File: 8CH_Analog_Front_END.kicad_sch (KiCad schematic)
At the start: 0 parts

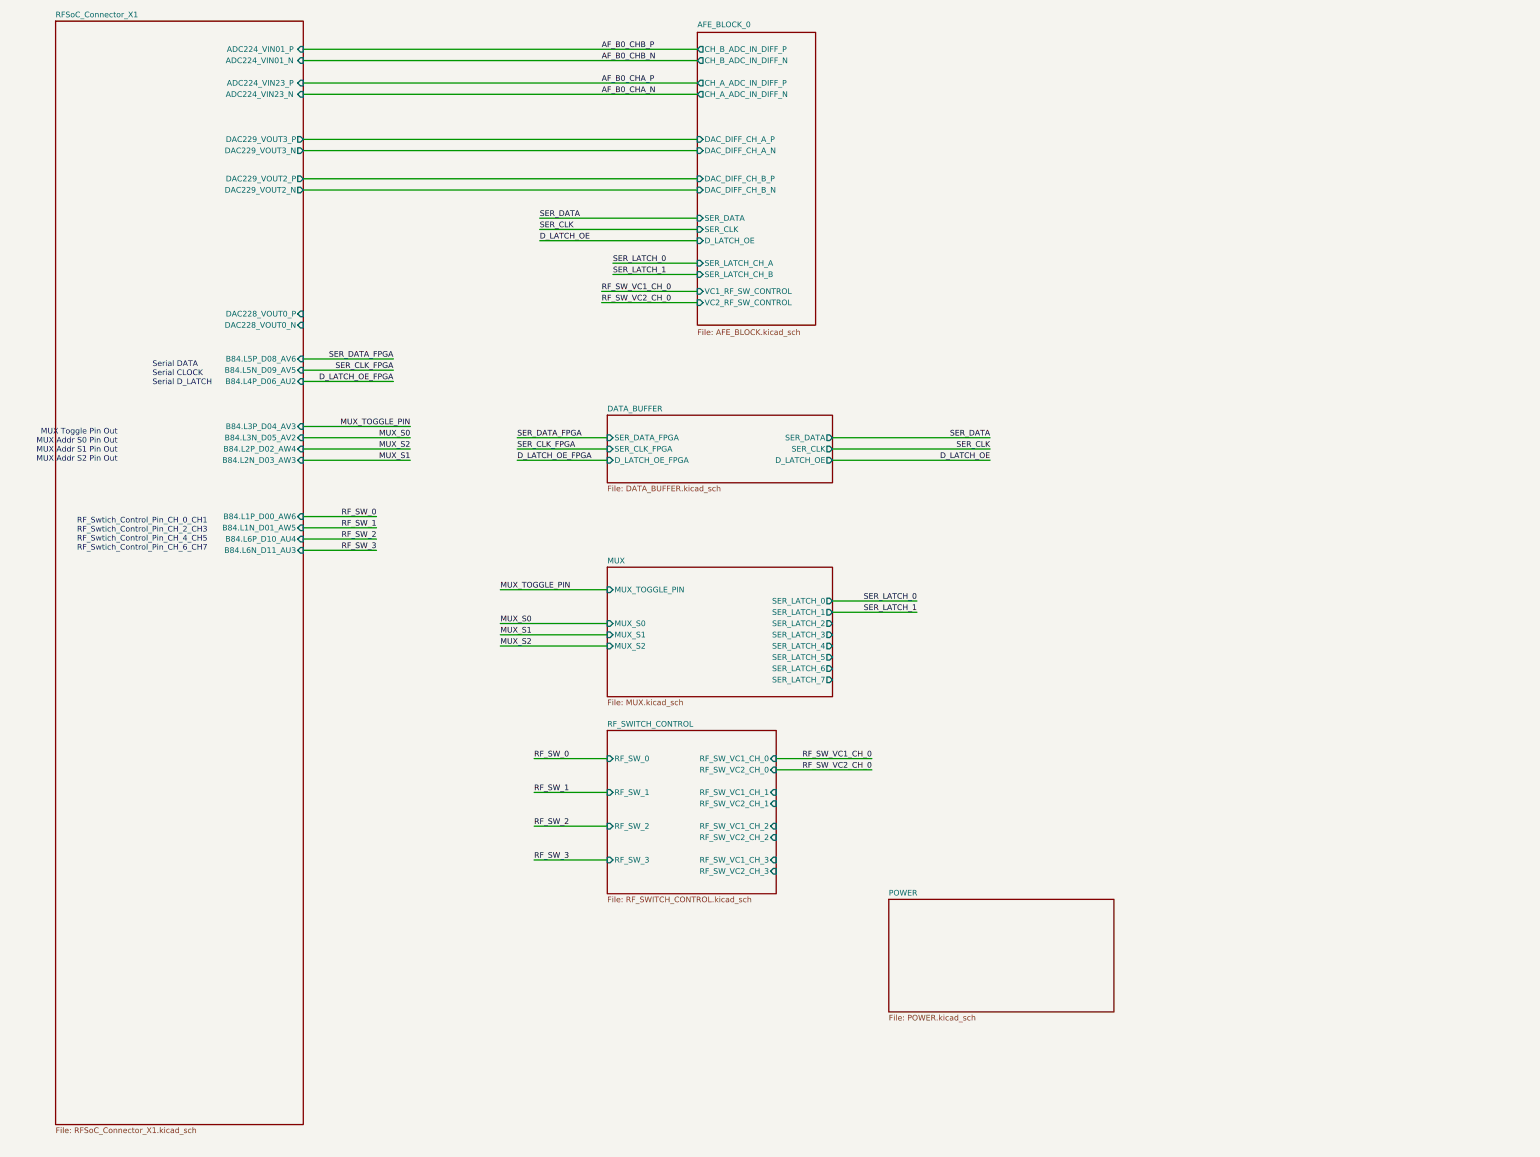
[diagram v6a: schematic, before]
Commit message: GND Vias added
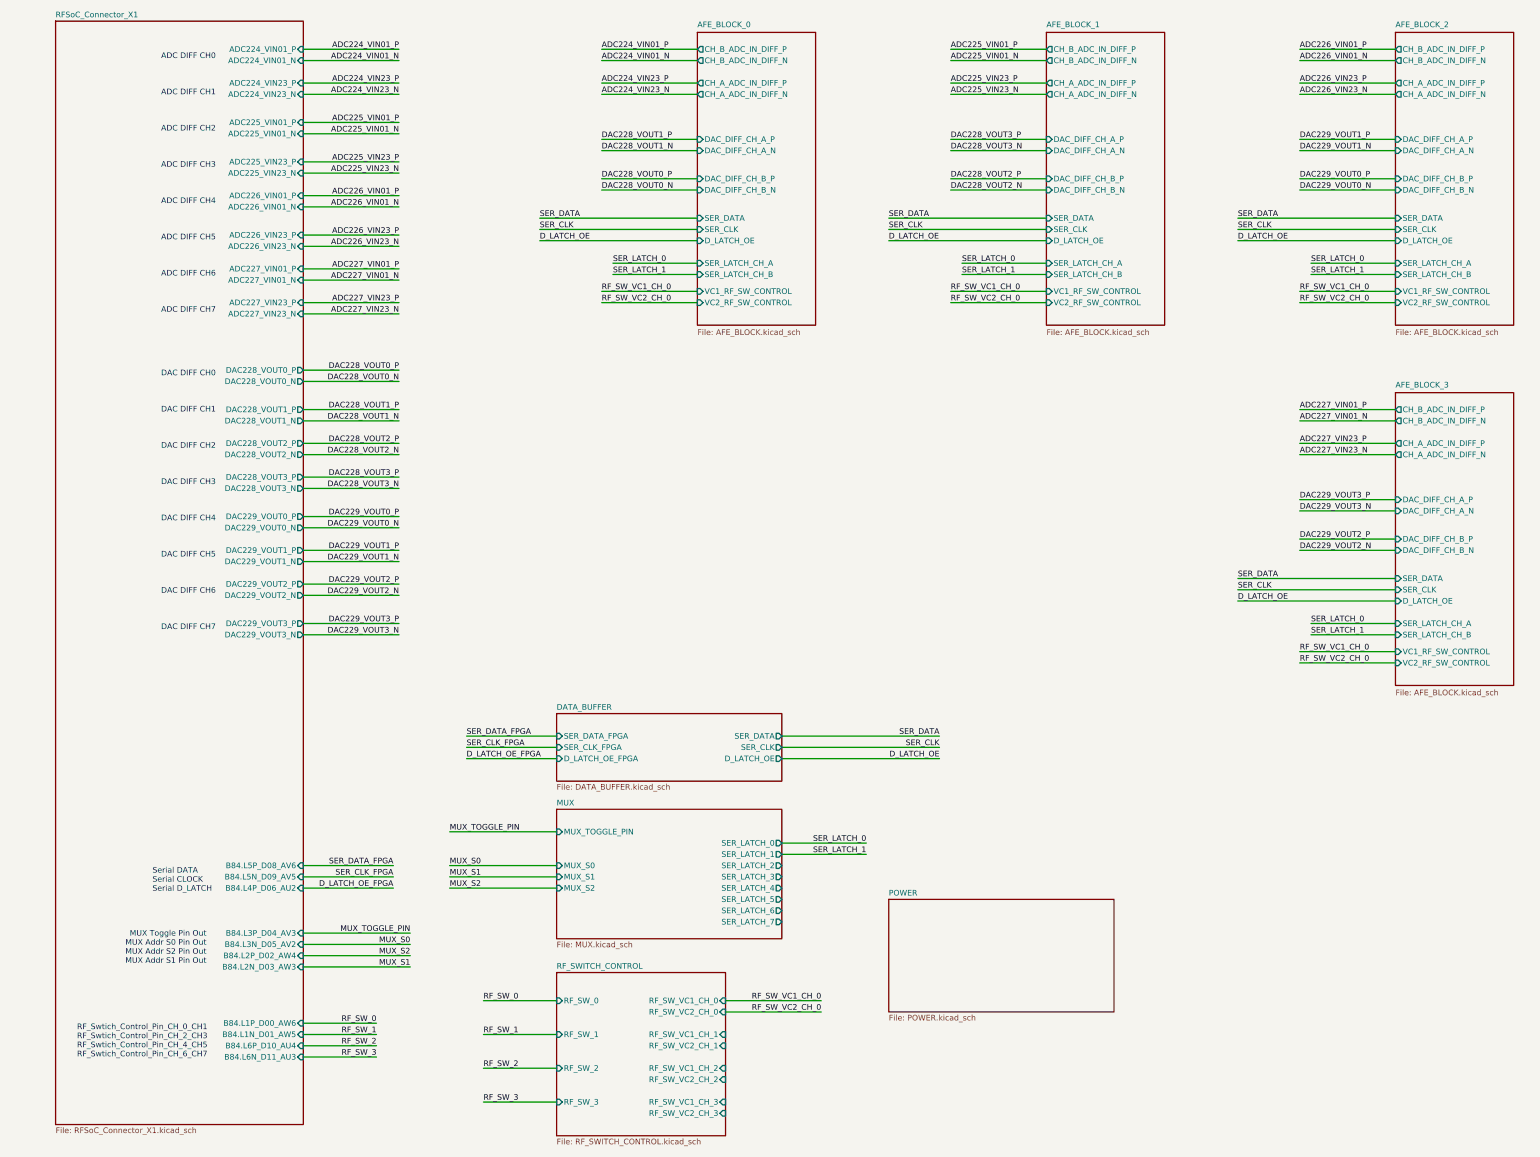
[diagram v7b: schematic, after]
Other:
- added sheet AFE_BLOCK_1 (AFE_BLOCK.kicad_sch)
- added sheet AFE_BLOCK_2 (AFE_BLOCK.kicad_sch)
- added sheet AFE_BLOCK_3 (AFE_BLOCK.kicad_sch)
- sheet RFSoC_Connector_X1 ports: added ADC224_VIN01_N, ADC224_VIN01_P, ADC224_VIN23_N, ADC224_VIN23_P, ADC225_VIN01_N, ADC225_VIN01_P, ADC225_VIN23_N, ADC225_VIN23_P, ADC226_VIN01_N, ADC226_VIN01_P, ADC226_VIN23_N, ADC226_VIN23_P, ADC227_VIN01_N, ADC227_VIN01_P, ADC227_VIN23_N, ADC227_VIN23_P, DAC228_VOUT1_N, DAC228_VOUT1_P, DAC228_VOUT2_N, DAC228_VOUT2_P, DAC228_VOUT3_N, DAC228_VOUT3_P, DAC229_VOUT0_N, DAC229_VOUT0_P, DAC229_VOUT1_N, DAC229_VOUT1_P; removed ADC224_VIN01_N , ADC224_VIN01_P , ADC224_VIN23_N , ADC224_VIN23_P 
- note added: "ADC DIFF CH0 ADC DIFF CH1 ADC DIFF CH2 ADC DIFF CH3 ADC DIFF CH4 ADC DIFF CH5 ADC DIFF CH6 ADC DIFF CH7 DAC DIFF CH0 DAC DIFF CH1 DAC DIFF CH2 DAC DIFF CH3 DAC DIFF CH4 DAC DIFF CH5 DAC DIFF CH6 DAC DIFF CH7"
- note added: "MUX Toggle Pin Out MUX Addr S0 Pin Out MUX Addr S2 Pin Out MUX Addr S1 Pin Out"
- note removed: "MUX Toggle Pin Out MUX Addr S0 Pin Out MUX Addr S1 Pin Out MUX Addr S2 Pin Out"
